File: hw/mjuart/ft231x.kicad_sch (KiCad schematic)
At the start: 5 parts, among them J1 S4B-ZR-SM4A-TFLFSN, J3 Conn_01x04_Pin, J4 Conn_01x04_Pin, U1 FT231XQ

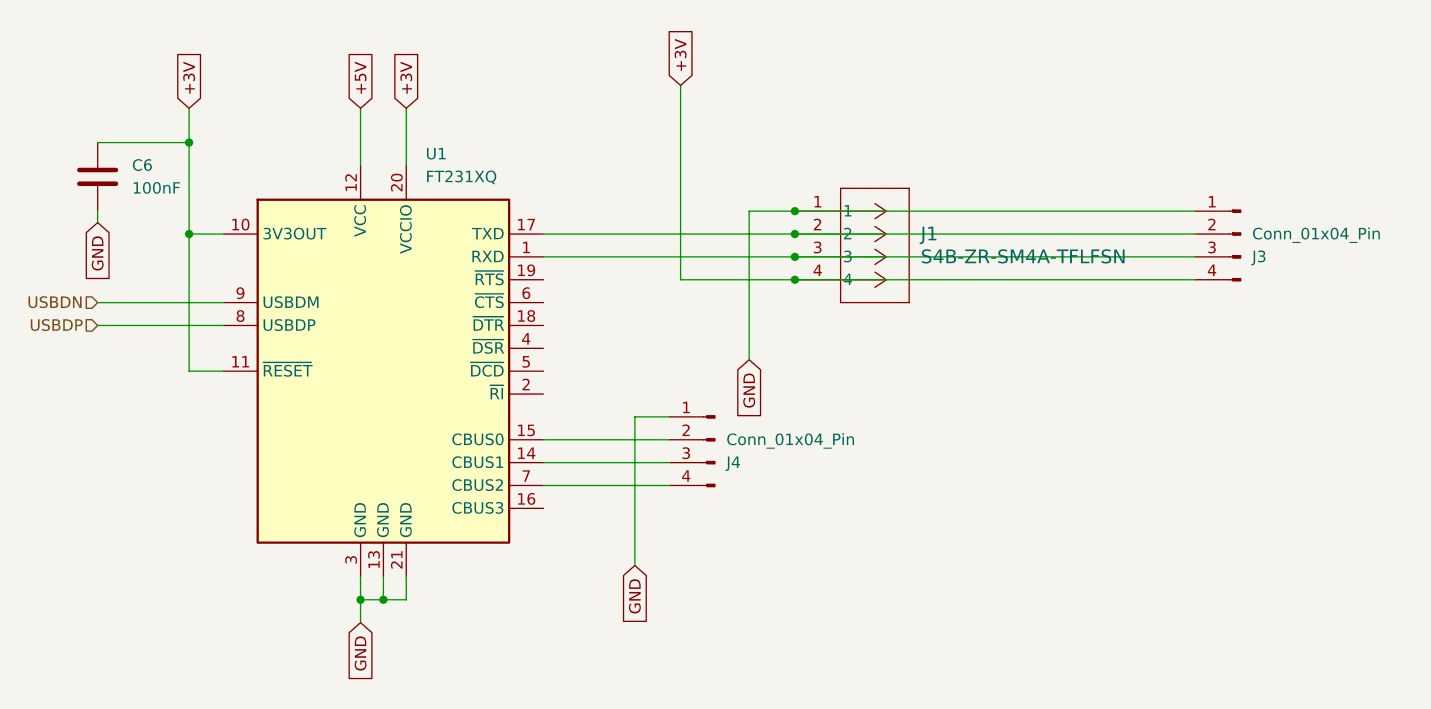
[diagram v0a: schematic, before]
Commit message: mjuart: Fill in all BOM entries and slight layout tweaks
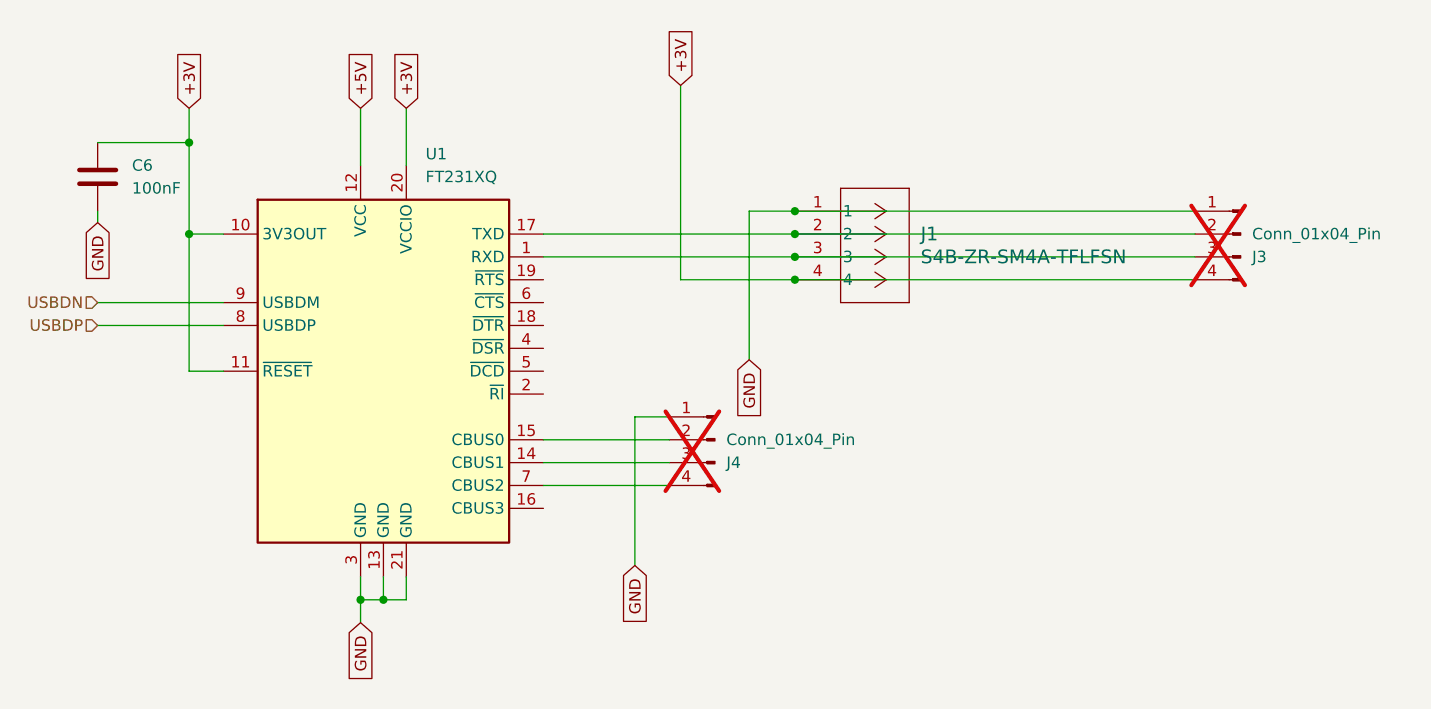
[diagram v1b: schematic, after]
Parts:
- C6: MPN (none) -> MF-CAP-0603-0.1uF
- J1: MF (none) -> JST; MPN (none) -> S4B-ZR-SM4A-TF(LF)(SN)
- J3, J4: now not fitted; now left out of the parts list
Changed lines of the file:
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@@
 		(unit 1)
 		(exclude_from_sim no)
-		(in_bom yes)
-		(on_board yes)
-		(dnp no)
+		(in_bom no)
+		(on_board yes)
+		(dnp yes)
 		(property "Reference" "J4"
 			(at 137.16 93.9801 0)
@@
 			)
 		)
-		(property "MPN" ""
+		(property "MPN" "MF-CAP-0603-0.1uF"
 			(at 67.31 62.23 0)
 			(effects
@@
 		(unit 1)
 		(exclude_from_sim no)
-		(in_bom yes)
-		(on_board yes)
-		(dnp no)
+		(in_bom no)
+		(on_board yes)
+		(dnp yes)
 		(property "Reference" "J3"
 			(at 195.58 71.1201 0)
@@
 			(at 144.78 66.04 0)
 			(effects
+				(font
+					(size 1.27 1.27)
+				)
+				(hide yes)
+			)
+		)
+		(property "MPN" "S4B-ZR-SM4A-TF(LF)(SN)"
+			(at 144.78 66.04 0)
+			(effects
+				(font
+					(size 1.27 1.27)
+				)
+				(hide yes)
+			)
+		)
+		(property "MF" "JST"
+			(at 144.78 66.04 0)
+			(effects

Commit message: mjuart: Fix all ERC and DRC violations
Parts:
- J1: footprint Connector_JST:JST_ZH_S4B-ZR-SM4A-TF_1x04-1MP_P1.50mm_Horizontal -> footprints:CONN_S4B-ZR-SM4A-TF_JST; symbol uart:S4B-ZR-SM4A-TFLFSN -> mjuart:S4B-ZR-SM4A-TFLFSN
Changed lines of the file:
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@@
 	)
 	(symbol
-		(lib_id "uart:S4B-ZR-SM4A-TFLFSN")
+		(lib_id "mjuart:S4B-ZR-SM4A-TFLFSN")
 		(at 144.78 66.04 0)
 		(unit 1)
@@
 			)
 		)
-		(property "Footprint" "Connector_JST:JST_ZH_S4B-ZR-SM4A-TF_1x04-1MP_P1.50mm_Horizontal"
+		(property "Footprint" "footprints:CONN_S4B-ZR-SM4A-TF_JST"
 			(at 144.78 66.04 0)
 			(effects

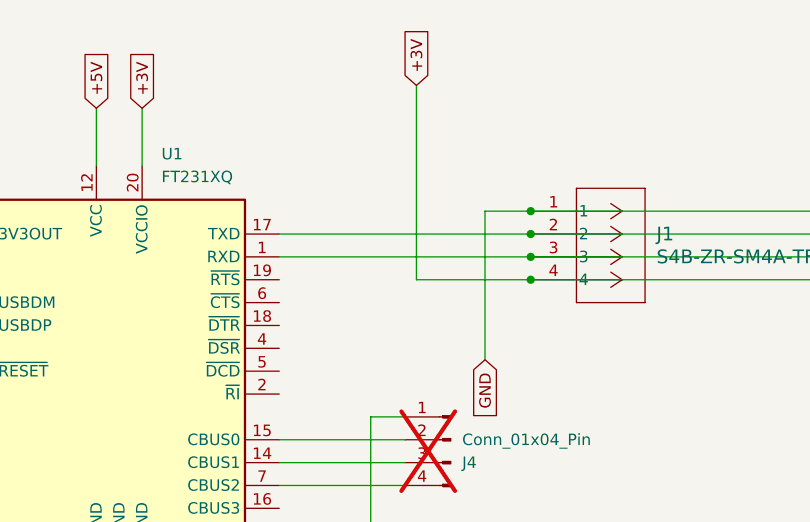
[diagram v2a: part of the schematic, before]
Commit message: mjuart: Fix ZH4 pinout to match moteus-r4
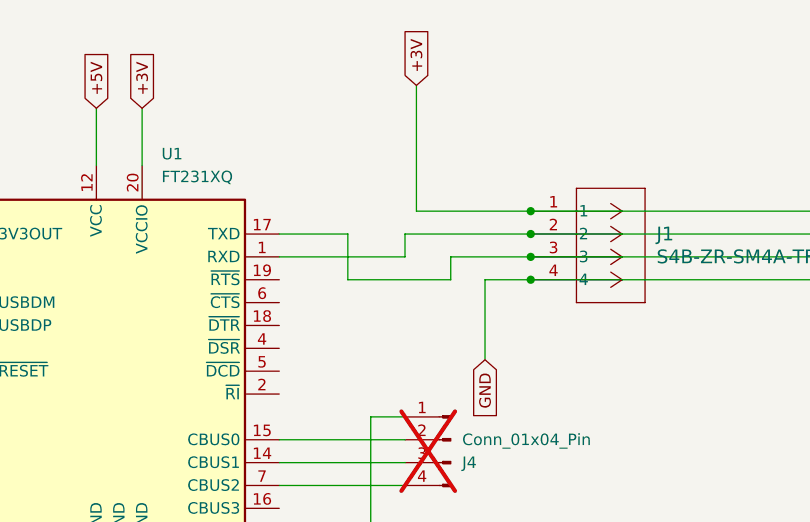
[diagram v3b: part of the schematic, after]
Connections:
- net +3V: now also J1.1, J3.1 (Pin_1); no longer J1.4, J3.4 (Pin_4)
- net GND: now also J1.4, J3.4 (Pin_4); no longer J1.1, J3.1 (Pin_1)
- net at J1.2, J3.2 (Pin_2): now also U1.1 (RXD); no longer U1.17 (TXD)
- net at J1.3, J3.3 (Pin_3): now also U1.17 (TXD); no longer U1.1 (RXD)
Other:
- title: mjuart r1 -> mjuart r2
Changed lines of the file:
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@@
 	(paper "A4")
 	(title_block
-		(title "mjuart r1")
+		(title "mjuart r2")
 		(company "mjbots Robotic Systems, LLC - info@mjbots.com")
 		(comment 1 "Licensed under the Apache 2.0 License")
 	)
 	(junction
+		(at 144.78 66.04)
+		(diameter 0)
+		(color 0 0 0 0)
+	)
+	(junction
 		(at 77.47 68.58)
 		(diameter 0)
@@
 	)
 	(junction
-		(at 144.78 66.04)
+		(at 144.78 71.12)
 		(diameter 0)
 		(color 0 0 0 0)
@@
 	)
 	(junction
+		(at 144.78 68.58)
+		(diameter 0)
+		(color 0 0 0 0)
+	)
+	(junction
+		(at 77.47 58.42)
+		(diameter 0)
+		(color 0 0 0 0)
+	)
+	(junction
+		(at 99.06 109.22)
+		(diameter 0)
+		(color 0 0 0 0)
+	)
+	(junction
 		(at 144.78 73.66)
 		(diameter 0)
 		(color 0 0 0 0)
 	)
-	(junction
-		(at 77.47 58.42)
-		(diameter 0)
-		(color 0 0 0 0)
-	)
-	(junction
-		(at 99.06 109.22)
-		(diameter 0)
-		(color 0 0 0 0)
-	)
-	(junction
-		(at 144.78 71.12)
-		(diameter 0)
-		(color 0 0 0 0)
-	)
-	(junction
-		(at 144.78 68.58)
-		(diameter 0)
-		(color 0 0 0 0)
-	)
-	(wire
-		(pts
-			(xy 144.78 73.66) (xy 132.08 73.66)
-		)
-		(stroke
-			(width 0)
-			(type default)
-		)
-	)
 	(wire
 		(pts
@@
 	(wire
 		(pts
-			(xy 116.84 71.12) (xy 144.78 71.12)
-		)
-		(stroke
-			(width 0)
-			(type default)
-		)
-	)
-	(wire
-		(pts
 			(xy 144.78 71.12) (xy 189.23 71.12)
 		)
@@
 	(wire
 		(pts
+			(xy 132.08 52.07) (xy 132.08 66.04)
+		)
+		(stroke
+			(width 0)
+			(type default)
+		)
+	)
+	(wire
+		(pts
 			(xy 77.47 68.58) (xy 77.47 83.82)
 		)
@@
 	(wire
 		(pts
+			(xy 130.81 68.58) (xy 144.78 68.58)
+		)
+		(stroke
+			(width 0)
+			(type default)
+		)
+	)
+	(wire
+		(pts
 			(xy 101.6 106.68) (xy 101.6 109.22)
 		)
@@
 	(wire
 		(pts
-			(xy 116.84 68.58) (xy 144.78 68.58)
+			(xy 130.81 71.12) (xy 130.81 68.58)
+		)
+		(stroke
+			(width 0)
+			(type default)
+		)
+	)
+	(wire
+		(pts
+			(xy 124.46 73.66) (xy 135.89 73.66)
+		)
+		(stroke
+			(width 0)
+			(type default)
+		)
+	)
+	(wire
+		(pts
+			(xy 124.46 68.58) (xy 124.46 73.66)
+		)
+		(stroke
+			(width 0)
+			(type default)
+		)
+	)
+	(wire
+		(pts
+			(xy 135.89 73.66) (xy 135.89 71.12)
+		)
+		(stroke
+			(width 0)
+			(type default)
+		)
+	)
+	(wire
+		(pts
+			(xy 139.7 73.66) (xy 144.78 73.66)
 		)
 		(stroke
@@
 	(wire
 		(pts
+			(xy 116.84 68.58) (xy 124.46 68.58)
+		)
+		(stroke
+			(width 0)
+			(type default)
+		)
+	)
+	(wire
+		(pts
 			(xy 127 88.9) (xy 127 105.41)
 		)
@@
 	(wire
 		(pts
-			(xy 144.78 66.04) (xy 139.7 66.04)
-		)
-		(stroke
-			(width 0)
-			(type default)
-		)
-	)
-	(wire
-		(pts
-			(xy 139.7 66.04) (xy 139.7 82.55)
+			(xy 116.84 71.12) (xy 130.81 71.12)
 		)
 		(stroke
@@
 	(wire
 		(pts
-			(xy 132.08 73.66) (xy 132.08 52.07)
+			(xy 139.7 82.55) (xy 139.7 73.66)
+		)
+		(stroke
+			(width 0)
+			(type default)
+		)
+	)
+	(wire
+		(pts
+			(xy 135.89 71.12) (xy 144.78 71.12)
 		)
 		(stroke
@@
 		)
 		(stroke
+			(width 0)
+			(type default)
+		)
+	)
+	(wire
+		(pts
+			(xy 132.08 66.04) (xy 144.78 66.04)
+		)
+		(stroke
